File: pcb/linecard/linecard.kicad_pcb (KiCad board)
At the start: 6 copper layers, 185 x 93.5 mm, 624 parts, among them J1 CONN_ATX12V, J10 ARF6-08-S-D-A-K-TR, J11 SMPM, J12 SMPM, J13 XILINX_JTAG, J14 ARF6-08-S-D-A-K-TR, J2 LPJT476156AENL, J3 CORTEX_DEBUG_ETM, J4 0532611071, J5 LPJT476156AENL, J6 XILINX_JTAG, J7 SMPM, J8 SMPM, J9 LPJT476156AENL, M1 LONGTHING, M10 SCREWHOLE, M11 SCREWHOLE, M12 960-27-12-D-AB-0, M13 960-27-12-D-AB-0, M2 OSHW, M3 WEEE, M4 SCREWHOLE, M5 SCREWHOLE, M6 SCREWHOLE, M7 SCREWHOLE, M8 SCREWHOLE, M9 SCREWHOLE, SW1 SWITCH, SW2 SWITCH, U1 MYMGK00504ERSR, U10 VSC8512, U11 ESD224DQAR, U12 ESD224DQAR, U13 ESD224DQAR, U14 ESD224DQAR, U15 ESD224DQAR, U16 ESD224DQAR, U17 ESD224DQAR, U18 ESD224DQAR, U19 ESD224DQAR, U2 MYMGK00504ERSR, U20 ESD224DQAR, U21 ESD224DQAR, U22 ESD224DQAR, U23 ESD224DQAR, U24 ESD224DQAR, U25 ESD224DQAR, U26 ESD224DQAR, U27 ESD224DQAR, U28 ESD224DQAR, U29 ESD224DQAR, U3 MYMGK00504ERSR, U30 ESD224DQAR, U31 ESD224DQAR, U32 ESD224DQAR, U33 ESD224DQAR, U34 ESD224DQAR, U35 VSC8512, U36 ESD224DQAR, U37 ESD224DQAR, U38 ESD224DQAR, U39 ESD224DQAR, U4 MYMGK00504ERSR, U40 ESD224DQAR, U41 ESD224DQAR, U42 ESD224DQAR, U43 ESD224DQAR, U44 ESD224DQAR, U45 ESD224DQAR, U46 ESD224DQAR, U47 ESD224DQAR, U48 ESD224DQAR, U49 ESD224DQAR, U5 STM32L431-QFN48, U50 ESD224DQAR, U51 ESD224DQAR, U52 ESD224DQAR, U53 ESD224DQAR, U54 ESD224DQAR, U55 ESD224DQAR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

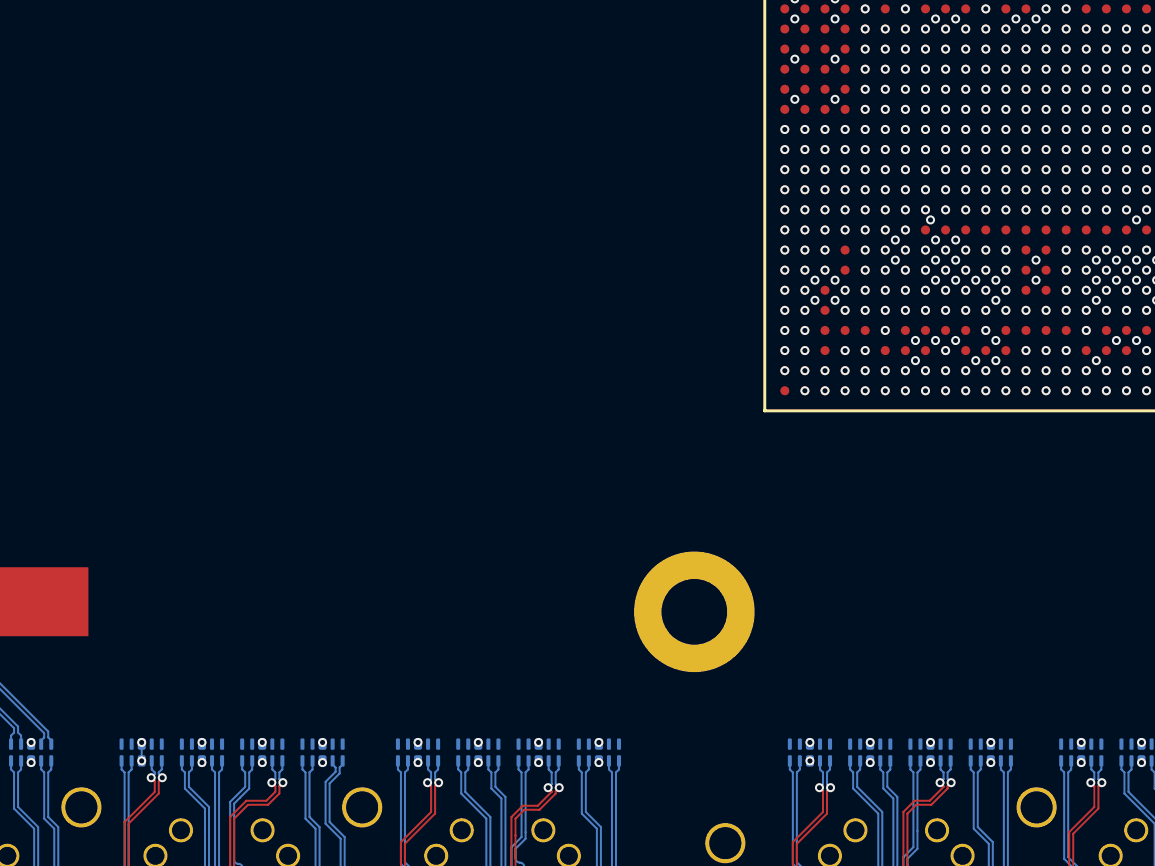
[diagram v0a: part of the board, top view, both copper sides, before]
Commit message: Continued routing right hand PHY
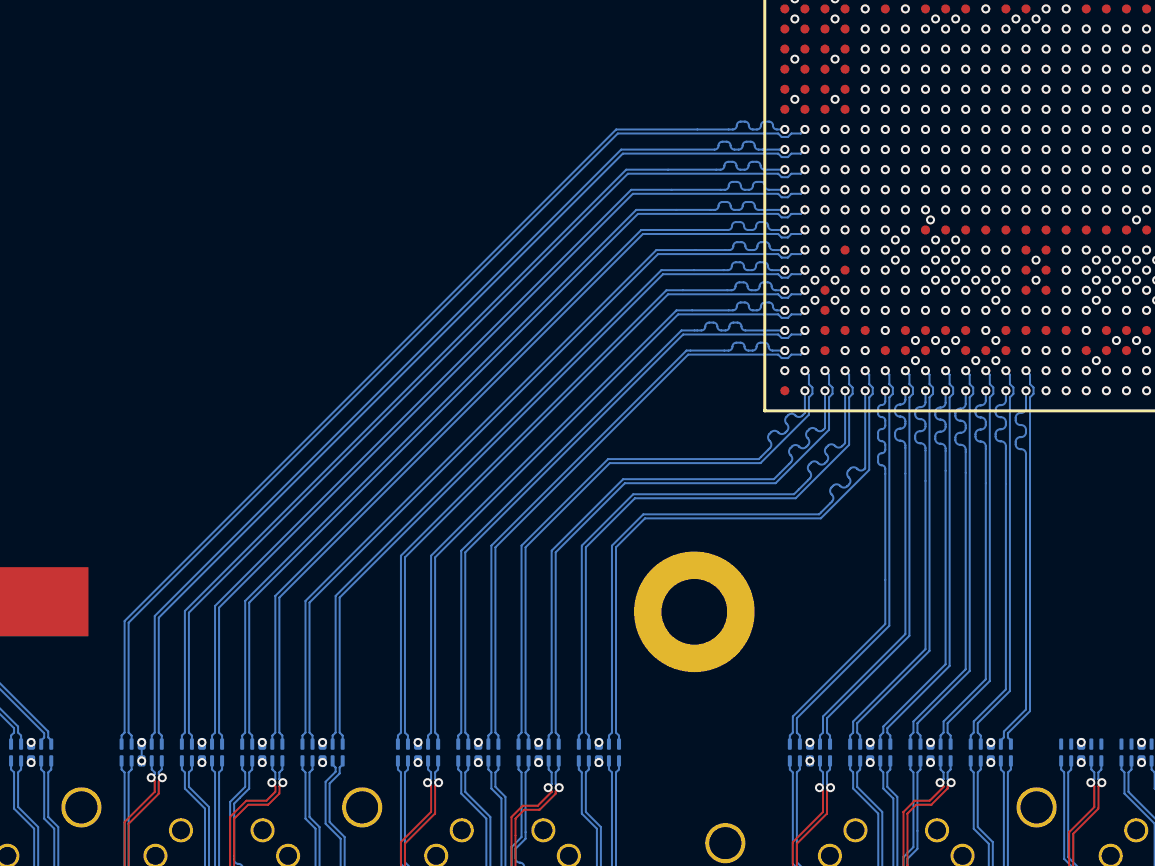
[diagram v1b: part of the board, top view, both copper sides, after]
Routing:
- net /PHY 1 MDI/PHY0_D3_N: track 0.00 -> 50.1 mm
- net /PHY 1 MDI/PHY0_D3_P: track 0.00 -> 50.0 mm
- net /PHY 1 MDI/PHY0_D2_N: track 0.00 -> 48.3 mm
- net /PHY 1 MDI/PHY0_D2_P: track 0.00 -> 48.2 mm
- net /PHY 1 MDI/PHY0_D1_N: track 0.00 -> 46.5 mm
- net /PHY 1 MDI/PHY0_D1_P: track 0.00 -> 46.5 mm
- net /PHY 1 MDI/PHY0_D0_N: track 0.00 -> 44.8 mm
- net /PHY 1 MDI/PHY0_D0_P: track 0.00 -> 44.7 mm
- net /PHY 1 MDI/PHY1_D3_N: track 0.00 -> 43.0 mm
- net /PHY 1 MDI/PHY1_D3_P: track 0.00 -> 42.9 mm
- net /PHY 1 MDI/PHY1_D2_N: track 0.00 -> 41.2 mm
- net /PHY 1 MDI/PHY1_D2_P: track 0.00 -> 41.2 mm
- net /PHY 1 MDI/PHY1_D1_N: track 0.00 -> 39.2 mm
- net /PHY 1 MDI/PHY1_D1_P: track 0.00 -> 39.1 mm
- net /PHY 1 MDI/PHY1_D0_N: track 0.00 -> 37.4 mm
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
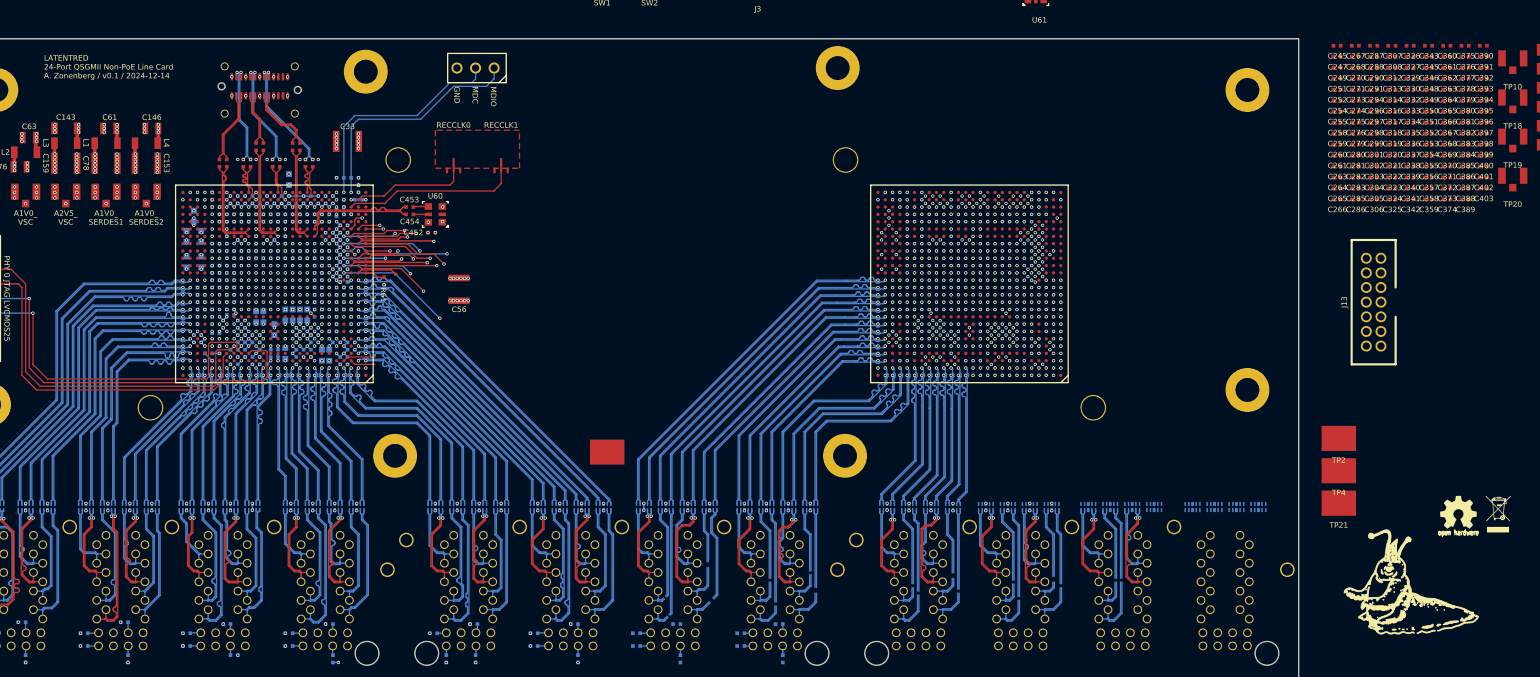
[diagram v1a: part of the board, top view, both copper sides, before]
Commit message: Continued routing right VSC8512
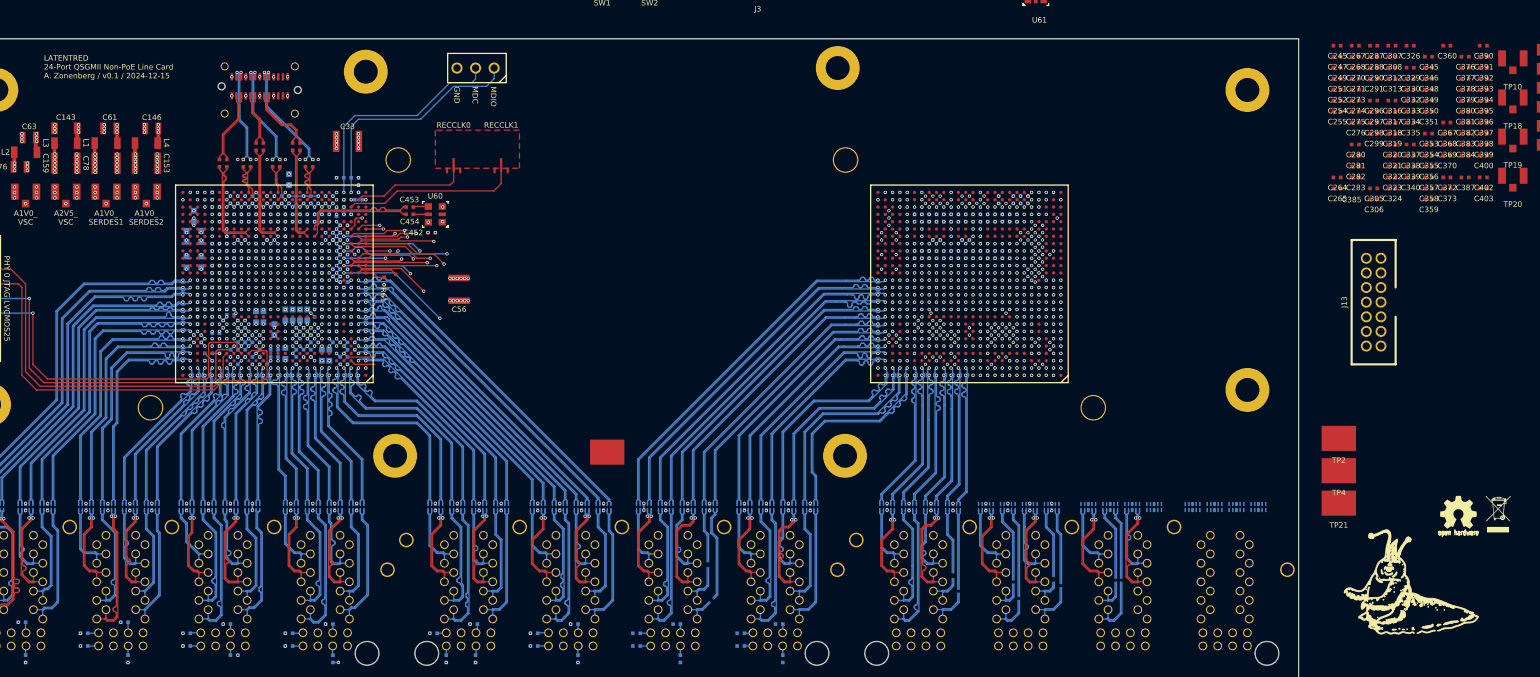
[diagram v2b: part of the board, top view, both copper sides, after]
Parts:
- C258, C259, C260, C261, C263, C266, C279, C285, C286, C294, C301, C302, C303, C304, C314, C325, C327, C336, C341, C342, C343, C352, C361, C362, C363, C364, C365, C366, C371, C374, C375, C386, C388, C389, C401: moved to B.Cu
- moved C375 73.1 mm to (167.5, 79.5), turned to -90 degrees
- moved C388 72.6 mm to (164.5, 82.5)
- moved C362 72.4 mm to (166.5, 84.5), turned to -90 degrees
- moved C363 71.0 mm to (167.5, 84.5), turned to -90 degrees
- moved C366 69.3 mm to (166.5, 79.5), turned to -90 degrees
- moved C389 68.5 mm to (168.5, 82.5), turned to 180 degrees
- moved C365 68.1 mm to (169.5, 84.5), turned to -90 degrees
- moved C364 67.6 mm to (170.5, 84.5), turned to -90 degrees
- moved C352 67.5 mm to (165.5, 79.5), turned to -90 degrees
- moved C336 65.8 mm to (164.5, 79.5), turned to -90 degrees
- moved C343 65.6 mm to (170.5, 79.5), turned to -90 degrees
- moved C361 65.6 mm to (172.5, 79.5), turned to -90 degrees
- moved C401 64.1 mm to (175.5, 79.5), turned to -90 degrees
- moved C304 62.6 mm to (162.5, 84.5), turned to -90 degrees
- moved C301 62.6 mm to (163.5, 84.5), turned to -90 degrees
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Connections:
- U36 pad 1: /PHY 1 MDI/PHY0_M0_N -> /PHY 1 MDI/PHY0_M0_P
- U36 pad 10: /PHY 1 MDI/PHY0_D0_N -> /PHY 1 MDI/PHY0_D0_P
- U36 pad 2: /PHY 1 MDI/PHY0_M0_P -> /PHY 1 MDI/PHY0_M0_N
- U36 pad 4: /PHY 1 MDI/PHY0_M1_N -> /PHY 1 MDI/PHY0_M1_P
- U36 pad 5: /PHY 1 MDI/PHY0_M1_P -> /PHY 1 MDI/PHY0_M1_N
- U36 pad 6: /PHY 1 MDI/PHY0_D1_P -> /PHY 1 MDI/PHY0_D1_N
- U36 pad 7: /PHY 1 MDI/PHY0_D1_N -> /PHY 1 MDI/PHY0_D1_P
- U36 pad 9: /PHY 1 MDI/PHY0_D0_P -> /PHY 1 MDI/PHY0_D0_N
- U40 pad 1: /PHY 1 MDI/PHY2_M0_N -> /PHY 1 MDI/PHY2_M0_P
- U40 pad 10: /PHY 1 MDI/PHY2_D0_N -> /PHY 1 MDI/PHY2_D0_P
- U40 pad 2: /PHY 1 MDI/PHY2_M0_P -> /PHY 1 MDI/PHY2_M0_N
- U40 pad 4: /PHY 1 MDI/PHY2_M1_N -> /PHY 1 MDI/PHY2_M1_P
- U40 pad 5: /PHY 1 MDI/PHY2_M1_P -> /PHY 1 MDI/PHY2_M1_N
- U40 pad 6: /PHY 1 MDI/PHY2_D1_P -> /PHY 1 MDI/PHY2_D1_N
- U40 pad 7: /PHY 1 MDI/PHY2_D1_N -> /PHY 1 MDI/PHY2_D1_P
- U40 pad 9: /PHY 1 MDI/PHY2_D0_P -> /PHY 1 MDI/PHY2_D0_N
- U42 pad 1: /PHY 1 MDI/PHY3_M0_N -> /PHY 1 MDI/PHY3_M0_P
- U42 pad 10: /PHY 1 MDI/PHY3_D0_N -> /PHY 1 MDI/PHY3_D0_P
- U42 pad 2: /PHY 1 MDI/PHY3_M0_P -> /PHY 1 MDI/PHY3_M0_N
- U42 pad 4: /PHY 1 MDI/PHY3_M1_N -> /PHY 1 MDI/PHY3_M1_P
- U42 pad 5: /PHY 1 MDI/PHY3_M1_P -> /PHY 1 MDI/PHY3_M1_N
- U42 pad 6: /PHY 1 MDI/PHY3_D1_P -> /PHY 1 MDI/PHY3_D1_N
- U42 pad 7: /PHY 1 MDI/PHY3_D1_N -> /PHY 1 MDI/PHY3_D1_P
- U42 pad 9: /PHY 1 MDI/PHY3_D0_P -> /PHY 1 MDI/PHY3_D0_N
- U44 pad 1: /PHY 1 MDI/PHY4_M0_N -> /PHY 1 MDI/PHY4_M0_P
- U44 pad 10: /PHY 1 MDI/PHY4_D0_N -> /PHY 1 MDI/PHY4_D0_P
- U44 pad 2: /PHY 1 MDI/PHY4_M0_P -> /PHY 1 MDI/PHY4_M0_N
- U44 pad 4: /PHY 1 MDI/PHY4_M1_N -> /PHY 1 MDI/PHY4_M1_P
- U44 pad 5: /PHY 1 MDI/PHY4_M1_P -> /PHY 1 MDI/PHY4_M1_N
- U44 pad 6: /PHY 1 MDI/PHY4_D1_P -> /PHY 1 MDI/PHY4_D1_N
- U44 pad 7: /PHY 1 MDI/PHY4_D1_N -> /PHY 1 MDI/PHY4_D1_P
- U44 pad 9: /PHY 1 MDI/PHY4_D0_P -> /PHY 1 MDI/PHY4_D0_N
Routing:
- net /GND: track 1516.0 -> 1572.5 mm
- net /2V5: track 141.9 -> 163.9 mm
- net /PHY 1 MDI/PHY1_LED1_N: track 0.00 -> 1.19 mm
- net /PHY 1 MDI/PHY2_M1_N: track 14.4 -> 15.4 mm
- net /PHY 1 MDI/PHY4_M0_N: track 17.2 -> 18.1 mm
- net /PHY 1 MDI/PHY2_M0_N: track 17.4 -> 18.4 mm
- net /PHY 1 MDI/PHY4_M1_N: track 14.3 -> 15.3 mm
- net /PHY 1 MDI/PHY3_M0_N: track 15.7 -> 16.5 mm
- net /PHY 1 MDI/PHY3_M0_P: track 15.9 -> 16.6 mm
- net /PHY 1 MDI/PHY0_M1_N: track 14.5 -> 15.1 mm
- net /PHY 1 MDI/PHY0_M0_N: track 17.2 -> 17.9 mm
- net /PHY 1 MDI/PHY0_M1_P: track 14.6 -> 15.1 mm
- net /PHY 1 MDI/PHY0_M0_P: track 17.4 -> 17.9 mm
- net /PHY 1 MDI/PHY4_M1_P: track 14.8 -> 15.3 mm
- net /PHY 1 MDI/PHY4_M0_P: track 17.7 -> 18.2 mm
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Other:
- board text added: "LATENTRED 24-Port QSGMII Non-PoE Line Card A. Zonenberg / v0.1 / 2024-12-15"
- board text removed: "LATENTRED 24-Port QSGMII Non-PoE Line Card A. Zonenberg / v0.1 / 2024-12-14"

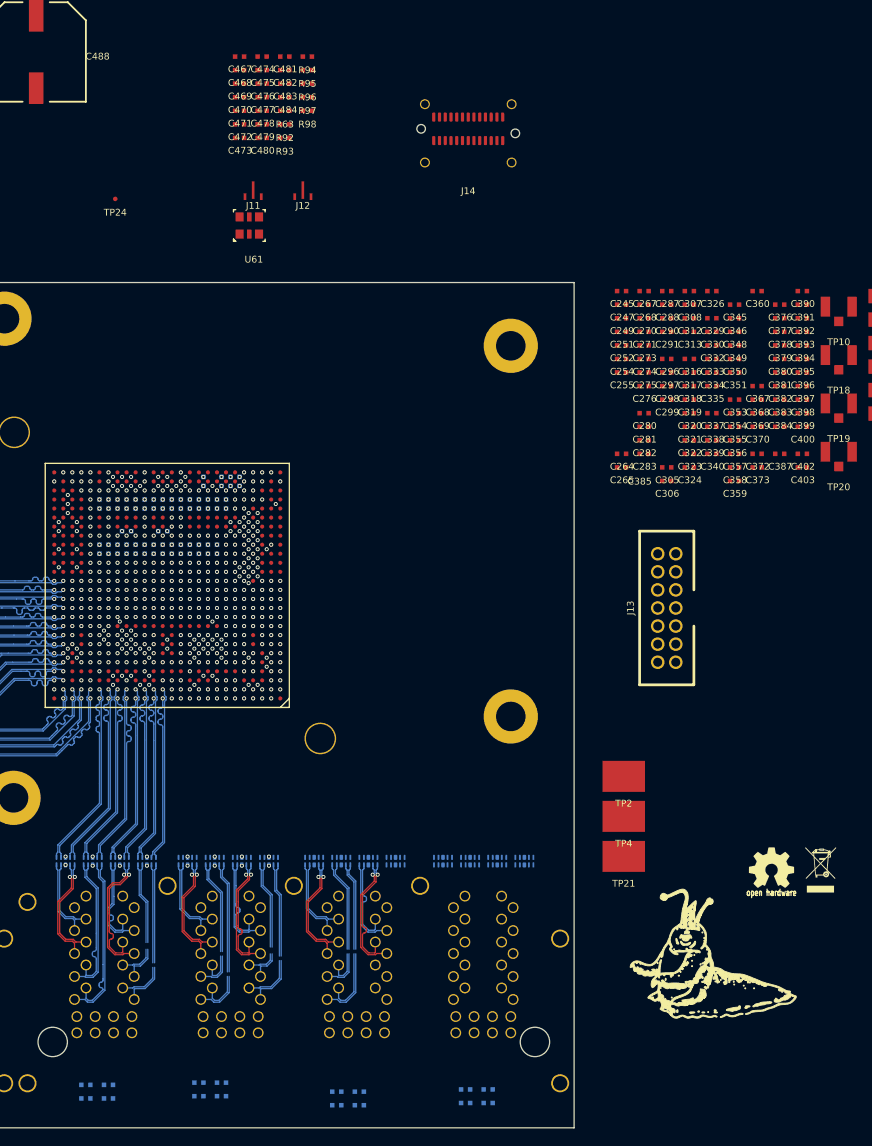
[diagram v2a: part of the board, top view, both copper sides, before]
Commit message: Continued routing right PHY power. 834 unrouted.
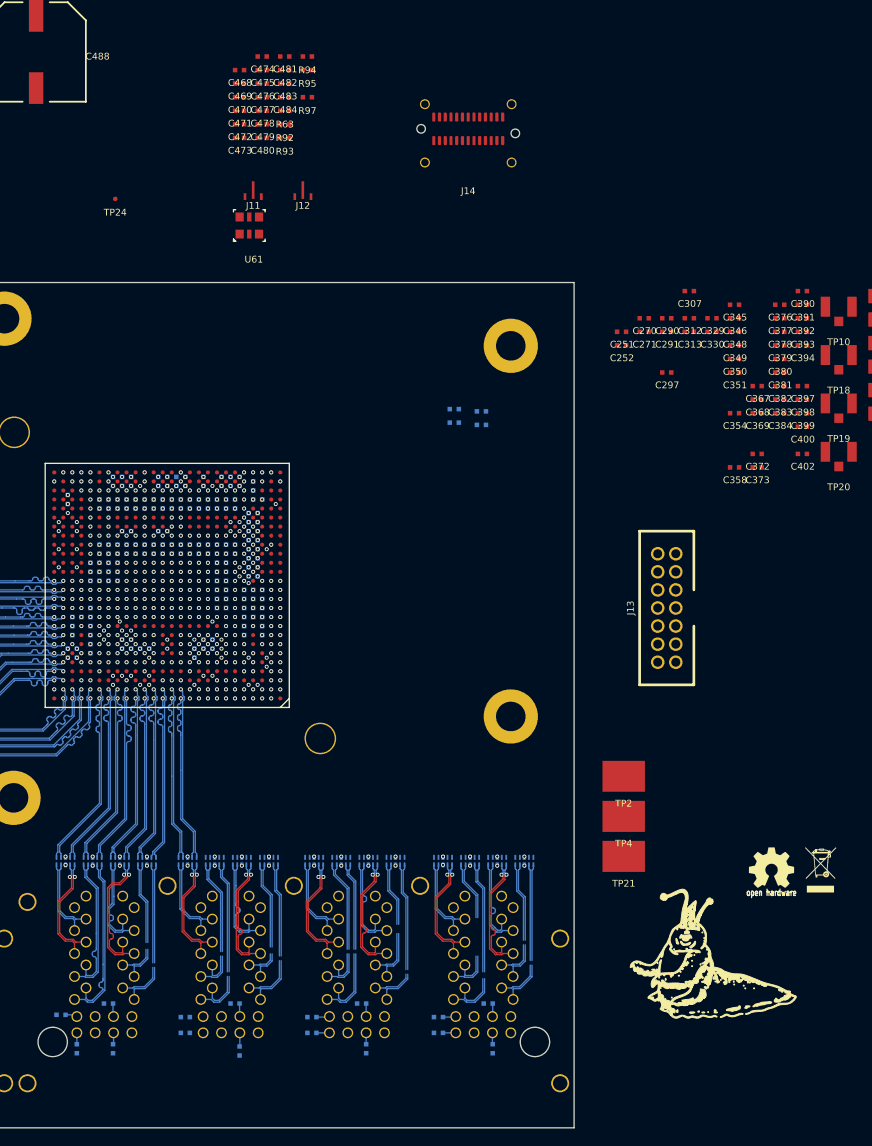
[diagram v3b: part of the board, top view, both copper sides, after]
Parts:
- C245, C247, C249, C254, C255, C264, C265, C267, C268, C273, C274, C275, C276, C280, C281, C282, C283, C287, C288, C296, C298, C299, C305, C306, C308, C316, C317, C318, C319, C320, C321, C322, C323, C324, C326, C332, C333, C334, C335, C337, C338, C339, C340, C353, C355, C356, C357, C359, C360, C370, C385, C387, C395, C396, C403, C467, R96, R98: moved to B.Cu
- moved C403 81.3 mm to (158.0, 79.0), turned to -90 degrees
- moved C395 77.4 mm to (163.0, 77.0), turned to 90 degrees
- moved C396 76.2 mm to (164.0, 77.0), turned to 90 degrees
- moved C359 75.8 mm to (158.5, 96.5), turned to 180 degrees
- moved C332 72.7 mm to (161.0, 87.0), turned to 180 degrees
- moved C334 72.0 mm to (161.0, 88.0), turned to 180 degrees
- moved C333 70.3 mm to (163.0, 87.0)
- moved C335 69.7 mm to (163.0, 88.0)
- moved C338 69.5 mm to (164.0, 95.0), turned to -90 degrees
- moved C298 69.3 mm to (160.5, 93.5), turned to -90 degrees
- moved C337 69.1 mm to (165.0, 95.0), turned to -90 degrees
- moved C317 69.0 mm to (161.0, 86.0), turned to 180 degrees
- moved C385 68.0 mm to (169.0, 77.0), turned to 90 degrees
- moved C299 68.0 mm to (160.5, 91.5), turned to 90 degrees
- moved C360 67.6 mm to (170.0, 77.0), turned to 90 degrees
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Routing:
- net /GND: track 1572.5 -> 1601.0 mm, vias 658 -> 674
- net /PHY 1 MDI/PHY6_D2_N: track 0.00 -> 19.5 mm
- net /PHY 1 MDI/PHY6_D2_P: track 0.00 -> 19.4 mm
- net /PHY 1 MDI/PHY6_D3_N: track 0.00 -> 19.2 mm
- net /PHY 1 MDI/PHY6_D3_P: track 0.00 -> 19.2 mm
- net /PHY 1 MDI/PHY10_M0_P: track 0.00 -> 17.8 mm
- net /PHY 1 MDI/PHY10_M0_N: track 0.00 -> 17.3 mm
- net /PHY 1 MDI/PHY9_M0_P: track 0.00 -> 16.3 mm
- net /PHY 1 MDI/PHY9_M0_N: track 0.00 -> 16.1 mm
- net /PHY 1 MDI/PHY11_M0_P: track 0.00 -> 15.7 mm
- net /PHY 1 MDI/PHY11_M0_N: track 0.00 -> 15.6 mm
- net /PHY 1 MDI/PHY11_M1_P: track 0.00 -> 13.2 mm
- net /PHY 1 MDI/PHY11_M1_N: track 0.00 -> 13.0 mm
- net /PHY 1 MDI/PHY11_M2_P: track 0.00 -> 13.0 mm, vias 0 -> 1
- net /PHY 1 MDI/PHY11_M2_N: track 0.00 -> 13.0 mm, vias 0 -> 1
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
